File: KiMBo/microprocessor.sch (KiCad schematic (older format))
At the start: 22 parts

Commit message: Update to use OSD335x as the main chipset
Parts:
- removed C? (x3): 1μF, symbol C
- removed C? (x3): 100nF, symbol C
- removed C?: 10nF, symbol C
- removed C? (x3): 10pF, symbol C
- removed C? (x2): 4.7μF, symbol C
- removed C? (x2): 18pF, symbol C
- removed L? (x2): 3.9nH, symbol INDUCTOR
- removed R? (x2): 4.7kΩ, symbol R
- removed R?: 22Ω, symbol R
- removed U? (x2): MT7620N, symbol MT7620N
- removed X?: 20MHz, symbol CRYSTAL-4
- added C? (x4): CP1, symbol CP1
- added R? (x2): R, symbol R
- added U? (x7): OSD3358, symbol OSD3358
- added Y? (x2): CRYSTAL, symbol CRYSTAL
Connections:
- net labels added: JTAG_FMJ0, JTAG_FMJ1, JTAG_TCK, JTAG_TDI, JTAG_TDO, JTAG_TMS, JTAG_TRSTN
- net labels removed: +1V2, +1V8, +3V3, 12S_CTRL, DDR_VREF, ERROR_LED, GND, MT_PLL_VC_CAP, MT_XTAL_XI, MT_XTAL_XO, RF0_V33N, RF1_V33N, ~PORST
- wire segments 111 -> 49
- no-connect marks 6 -> 1
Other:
- note added: "Analog I/O"
- note added: "EMMC04G-S100-B08U"
- note added: "GPMC"
- note added: "JTAG"
- note added: "LCD"

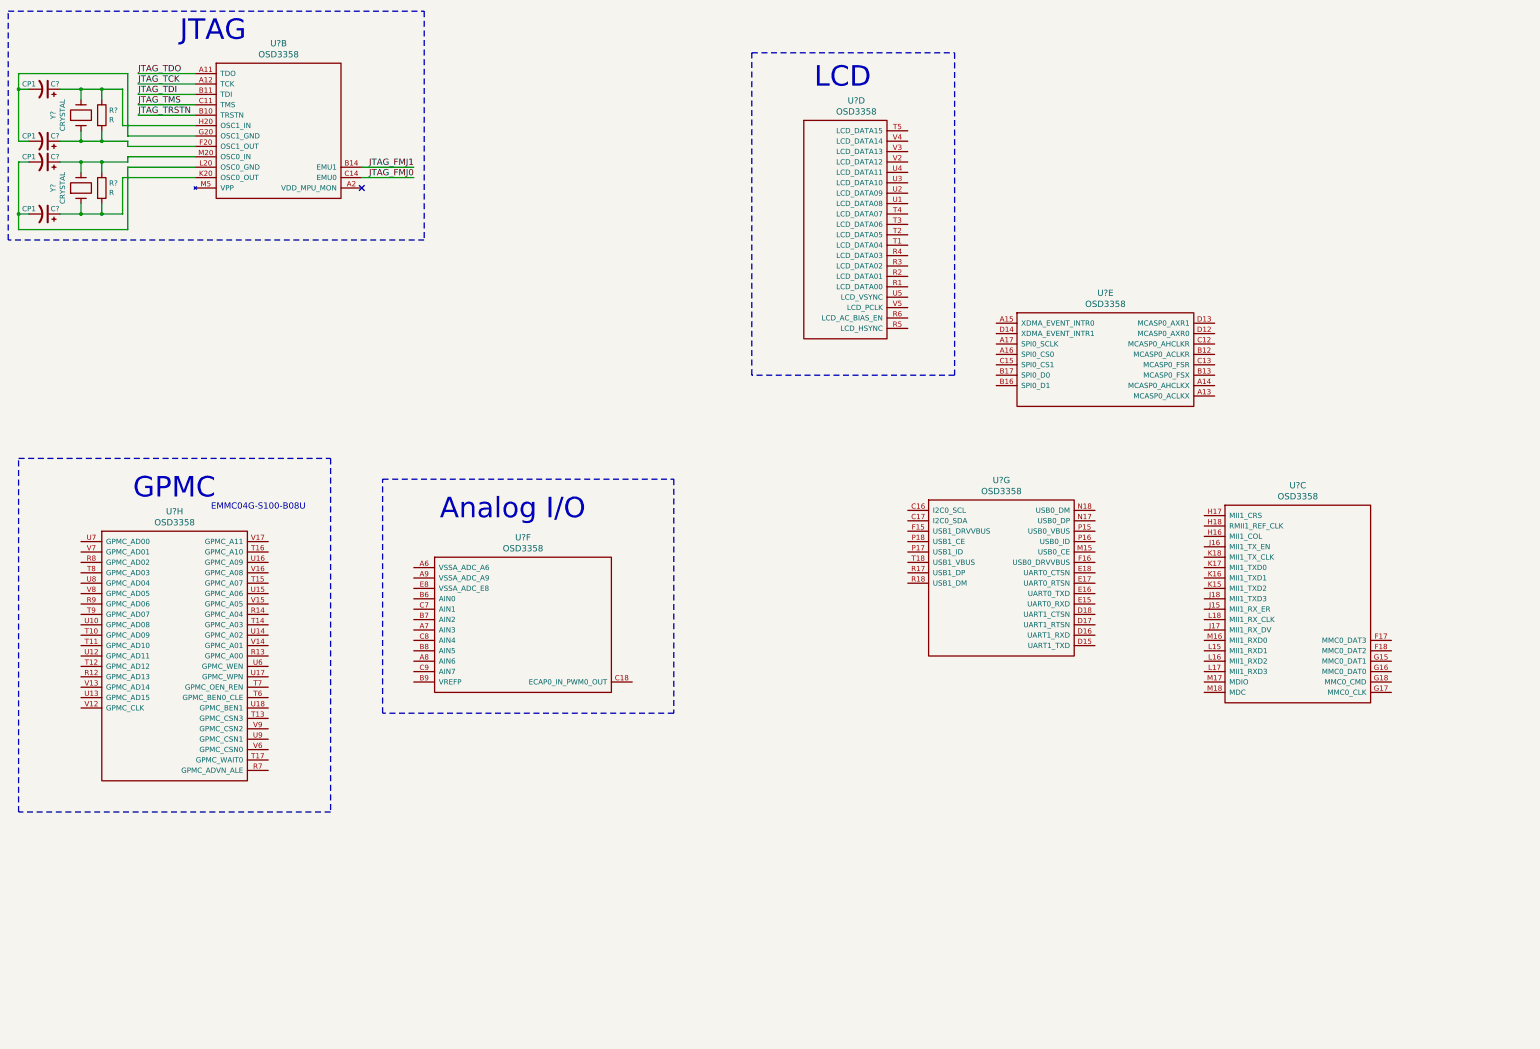
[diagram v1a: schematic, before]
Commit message: Move various symbols, add notes, add labels
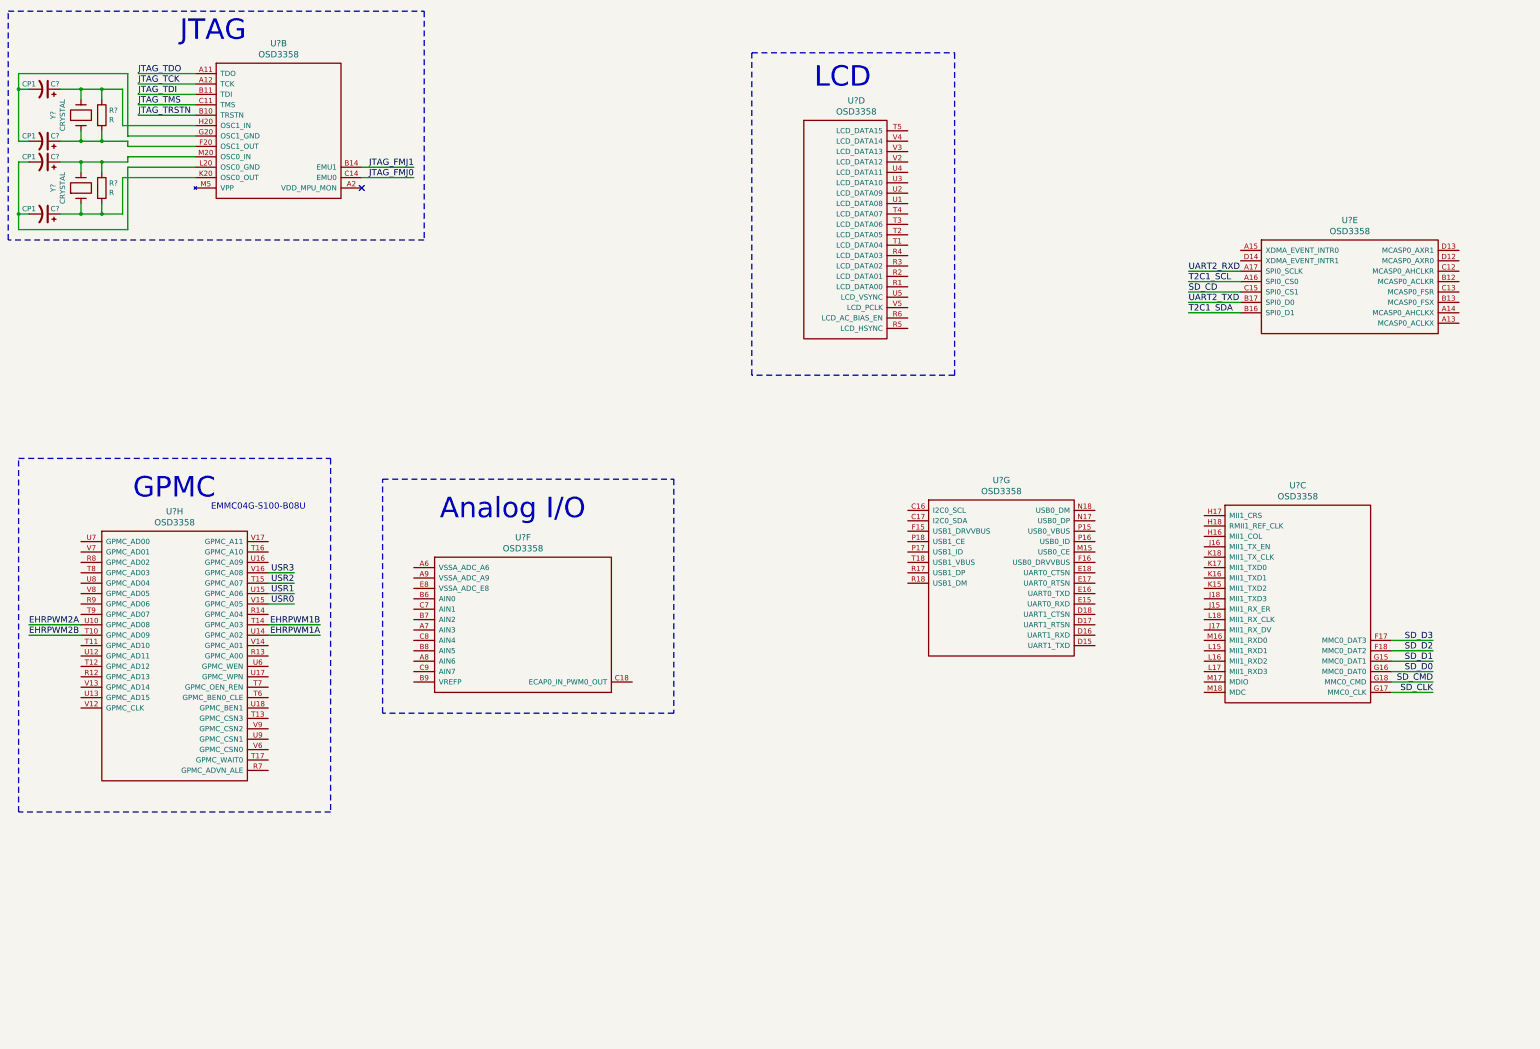
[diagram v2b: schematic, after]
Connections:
- net EHRPWM2B: now reaches U?.T10 (GPMC_AD09)
- net EHRPWM1B: now reaches U?.T14 (GPMC_A03)
- net USR2: now reaches U?.T15 (GPMC_A07)
- net EHRPWM2A: now reaches U?.U10 (GPMC_AD08)
- net EHRPWM1A: now reaches U?.U14 (GPMC_A02)
- net USR1: now reaches U?.U15 (GPMC_A06)
- net USR0: now reaches U?.V15 (GPMC_A05)
- net USR3: now reaches U?.V16 (GPMC_A08)
- net T2C1_SCL: now reaches U?.A16 (SPI0_CS0)
- net UART2_RXD: now reaches U?.A17 (SPI0_SCLK)
- net T2C1_SDA: now reaches U?.B16 (SPI0_D1)
- net UART2_TXD: now reaches U?.B17 (SPI0_D0)
- net SD_CD: now reaches U?.C15 (SPI0_CS1)
- net SD_D3: now reaches U?.F17 (MMC0_DAT3)
- net SD_D2: now reaches U?.F18 (MMC0_DAT2)
- net SD_D1: now reaches U?.G15 (MMC0_DAT1)
- net SD_D0: now reaches U?.G16 (MMC0_DAT0)
- net SD_CLK: now reaches U?.G17 (MMC0_CLK)
- net SD_CMD: now reaches U?.G18 (MMC0_CMD)
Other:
- moved on the sheet: U?E
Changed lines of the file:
@@
 L OSD3358 U?
 U 5 1 582FE5A0
-P 10250 3700
-F 0 "U?" H 11300 3990 60  0000 C CNN
-F 1 "OSD3358" H 11300 3884 60  0000 C CNN
-F 2 "" H 10250 3700 60  0001 C CNN
-F 3 "" H 10250 3700 60  0001 C CNN
-	5    10250 3700
+P 12600 3000
+F 0 "U?" H 13650 3290 60  0000 C CNN
+F 1 "OSD3358" H 13650 3184 60  0000 C CNN
+F 2 "" H 12600 3000 60  0001 C CNN
+F 3 "" H 12600 3000 60  0001 C CNN
+	5    12600 3000
 	1    0    0    -1
 $EndComp
@@
 	850  2650 950  2650
 Wire Wire Line
-	850  2150 850  2650
-Wire Wire Line
-	850  2650 850  2800
+	850  2150 850  2800
 Wire Wire Line
 	950  2150 850  2150
@@
 	850  1950 950  1950
 Wire Wire Line
-	850  1300 850  1450
-Wire Wire Line
-	850  1450 850  1950
+	850  1300 850  1950
 Wire Wire Line
 	850  1450 950  1450
@@
 $EndComp
 Wire Wire Line
-	1900 1950 1650 1950
-Wire Wire Line
-	1650 1950 1450 1950
-Wire Wire Line
-	1450 1950 1250 1950
-Wire Wire Line
-	1850 1450 1650 1450
-Wire Wire Line
-	1650 1450 1450 1450
-Wire Wire Line
-	1450 1450 1250 1450
-Wire Wire Line
-	1250 2650 1450 2650
-Wire Wire Line
-	1450 2650 1650 2650
-Wire Wire Line
-	1650 2650 1850 2650
-Wire Wire Line
-	1250 2150 1450 2150
-Wire Wire Line
-	1450 2150 1650 2150
-Wire Wire Line
-	1650 2150 1900 2150
+	1900 1950 1250 1950
+Wire Wire Line
+	1850 1450 1250 1450
+Wire Wire Line
+	1250 2650 1850 2650
+Wire Wire Line
+	1250 2150 1900 2150
 Wire Wire Line
 	1450 2250 1450 2150
@@
 	1450 1850 1450 1950
 Connection ~ 1450 1950
+Text Label 3500 6400 2    60   ~ 0
+USR0
+Text Label 3500 6300 2    60   ~ 0
+USR1
+Wire Wire Line
+	3500 6300 3250 6300
+Wire Wire Line
+	3250 6400 3500 6400
+Text Label 3500 6200 2    60   ~ 0
+USR2
+Text Label 3500 6100 2    60   ~ 0
+USR3
+Wire Wire Line
+	3250 6100 3500 6100
+Wire Wire Line
+	3250 6200 3500 6200
+Text Label 12100 3200 0    60   ~ 0
+UART2_RXD
+Text Label 12100 3500 0    60   ~ 0
+UART2_TXD
+Wire Wire Line
+	12600 3200 12100 3200
+Wire Wire Line
+	12600 3500 12100 3500
+Text Label 12100 3600 0    60   ~ 0
+T2C1_SDA
+Wire Wire Line
+	12100 3600 12600 3600
+Text Label 12100 3300 0    60   ~ 0
+T2C1_SCL
+Wire Wire Line
+	12100 3300 12600 3300
+Text Label 950  6700 0    60   ~ 0
+EHRPWM2B
+Wire Wire Line
+	1450 6700 950  6700
+Text Label 950  6600 0    60   ~ 0
+EHRPWM2A
+Text Label 3750 6600 2    60   ~ 0
+EHRPWM1B
+Text Label 3750 6700 2    60   ~ 0
+EHRPWM1A
+Wire Wire Line
+	3750 6600 3250 6600
+Wire Wire Line
+	3750 6700 3250 6700
+Wire Wire Line
+	1450 6600 950  6600
+Text Label 14450 6750 2    60   ~ 0
+SD_D3
+Text Label 14450 6850 2    60   ~ 0
+SD_D2
+Text Label 14450 6950 2    60   ~ 0
+SD_D1
+Text Label 14450 7050 2    60   ~ 0
+SD_D0
+Text Label 14450 7150 2    60   ~ 0
+SD_CMD
+Text Label 14450 7250 2    60   ~ 0
+SD_CLK
+Text Label 12100 3400 0    60   ~ 0
+SD_CD
+Wire Wire Line
+	12100 3400 12600 3400
+Wire Wire Line
+	14450 6750 14050 6750
+Wire Wire Line
+	14450 6850 14050 6850
+Wire Wire Line
+	14450 6950 14050 6950
+Wire Wire Line
+	14450 7050 14050 7050
+Wire Wire Line
+	14450 7150 14050 7150
+Wire Wire Line
+	14450 7250 14050 7250
 $EndSCHEMATC

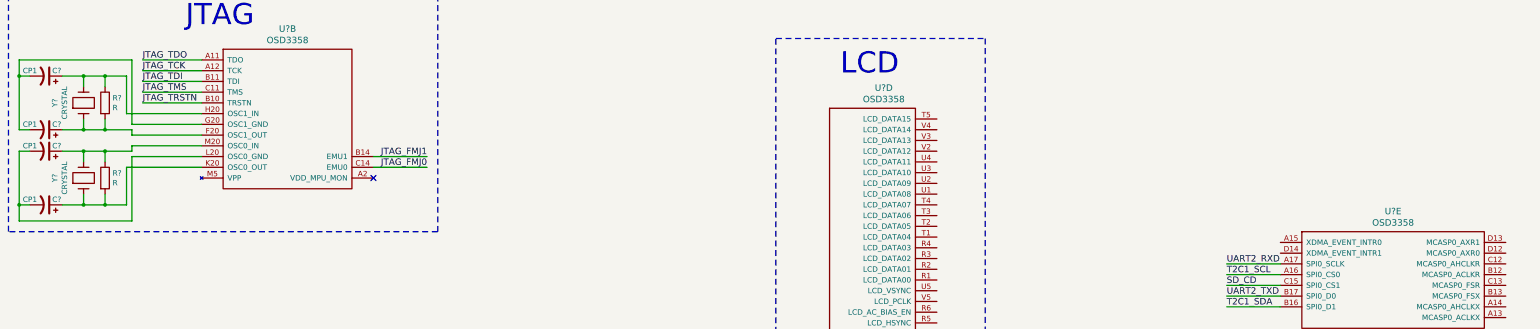
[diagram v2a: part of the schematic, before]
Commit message: Update the schematic with various nets and labels
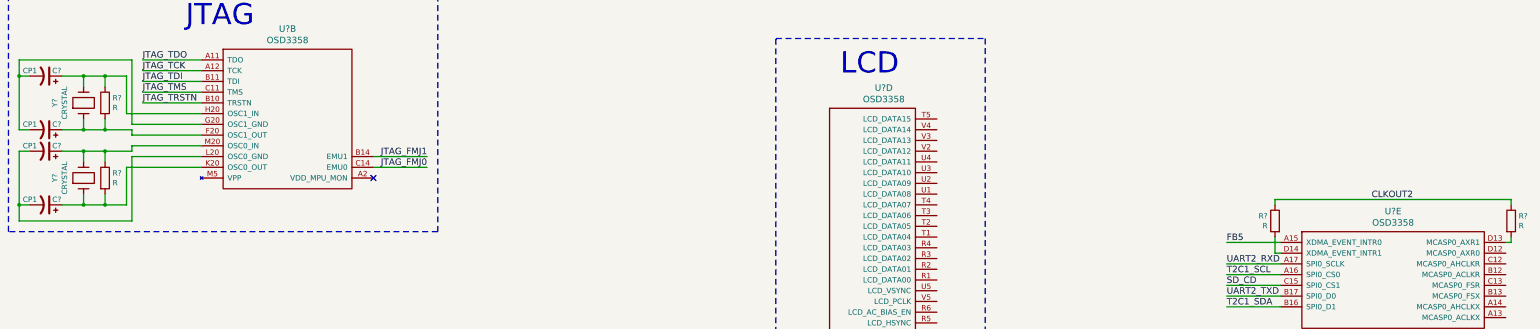
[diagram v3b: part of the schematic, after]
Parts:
- added R? (x2): R, symbol R
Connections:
- net FB5: now reaches U?.A15 (XDMA_EVENT_INTR0)
- net at U?.D13 (MCASP0_AXR1): now also R?.2
- net at U?.D14 (XDMA_EVENT_INTR1): now also R?.2
- new net CLKOUT2: R?.1, R?.1
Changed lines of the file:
@@
 	2550 2000 1900 2000
 Wire Wire Line
-	1900 2000 1900 1950
+	1900 1950 1900 2000
 Wire Wire Line
 	1900 2150 1900 2100
@@
 	2550 1800 1850 1800
 Wire Wire Line
-	1850 1800 1850 1450
+	1850 1450 1850 1800
 Wire Wire Line
 	1650 1550 1650 1450
@@
 $EndComp
 Wire Wire Line
-	1900 1950 1250 1950
-Wire Wire Line
-	1850 1450 1250 1450
+	1250 1950 1900 1950
+Wire Wire Line
+	1250 1450 1850 1450
 Wire Wire Line
 	1250 2650 1850 2650
@@
 Wire Wire Line
 	14450 7250 14050 7250
+$Comp
+L R R?
+U 1 1 5834D6F6
+P 14750 2800
+F 0 "R?" H 14820 2846 50  0000 L CNN
+F 1 "R" H 14820 2755 50  0000 L CNN
+F 2 "" V 14680 2800 50  0000 C CNN
+F 3 "" H 14750 2800 50  0000 C CNN
+	1    14750 2800
+	1    0    0    -1
+$EndComp
+Wire Wire Line
+	14700 3000 14750 3000
+Wire Wire Line
+	14750 3000 14750 2950
+$Comp
+L R R?
+U 1 1 5834D7CD
+P 12550 2800
+F 0 "R?" H 12619 2846 50  0000 L CNN
+F 1 "R" H 12619 2755 50  0000 L CNN
+F 2 "" V 12480 2800 50  0000 C CNN
+F 3 "" H 12550 2800 50  0000 C CNN
+	1    12550 2800
+	-1   0    0    -1
+$EndComp
+Wire Wire Line
+	12600 3100 12550 3100
+Wire Wire Line
+	12550 3100 12550 2950
+Wire Wire Line
+	12550 2650 12550 2600
+Wire Wire Line
+	12550 2600 14750 2600
+Wire Wire Line
+	14750 2600 14750 2650
+Text Label 13450 2600 0    60   ~ 0
+CLKOUT2
+Wire Wire Line
+	12600 3000 12100 3000
+Text Label 12100 3000 0    60   ~ 0
+FB5
 $EndSCHEMATC

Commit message: More updates to the schematics
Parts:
- added C?: C, symbol C
- added C? (x3): CP1, symbol CP1
- added OSC?: ASDMB, symbol ASDMB
- added P?: CONN_01X06, symbol CONN_01X06
- added R? (x18): R, symbol R
- added U?: 74LVC1G06, symbol 74LVC1G06
- added U?: 74LVC2G241, symbol 74LVC2G241
- added U?: 74LVC1G74, symbol 74LVC1G74
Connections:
- net FB5: now also R?.2
- net GPIO1_13: now reaches U?.R12 (GPMC_AD13)
- net GPIO1_16.SIP: now reaches U?.R13 (GPMC_A00)
- net GPIO1_16.SIP: now also R?.1
- net at U?.R14 (GPMC_A04): now also U?.2
- net TIMER4: now reaches U?.R7 (GPMC_ADVN_ALE)
- net MMC1_DAT2: now reaches U?.R8 (GPMC_AD02)
- net MMC1_DAT6: now reaches U?.R9 (GPMC_AD06)
- net GPIO0_26: now reaches U?.T11 (GPMC_AD10)
- net GPIO1_12: now reaches U?.T12 (GPMC_AD12)
- net GPIO2_0.SIP: now reaches U?.T13 (GPMC_CSN3)
- net USB1_OC#: now reaches U?.T16 (GPMC_A10)
- net UART4_RXD: now reaches U?.T17 (GPMC_WAIT0)
- net TIMER5: now reaches U?.T6 (GPMC_BEN0_CLE)
- net TIMER7: now reaches U?.T7 (GPMC_OEN_REN)
- net MMC1_DAT3: now reaches U?.T8 (GPMC_AD03)
- net MMC1_DAT7: now reaches U?.T9 (GPMC_AD07)
- net GPIO0_27: now reaches U?.U12 (GPMC_AD11)
- net GPIO1_15: now reaches U?.U13 (GPMC_AD15)
- net HDMI_INT: now reaches U?.U16 (GPMC_A09)
- net UART4_TXD: now reaches U?.U17 (GPMC_WPN)
- net GPIO1_28: now reaches U?.U18 (GPMC_BEN1)
- net TIMER6: now reaches U?.U6 (GPMC_WEN)
- net MMC1_DAT0: now reaches U?.U7 (GPMC_AD00)
- net MMC1_DAT4: now reaches U?.U8 (GPMC_AD04)
- net MMC1_CLK: now reaches U?.U9 (GPMC_CSN1)
- net GPIO2_1: now reaches U?.V12 (GPMC_CLK)
- net GPIO1_14: now reaches U?.V13 (GPMC_AD14)
- net GPIO1_17: now reaches U?.V14 (GPMC_A01)
- net HDMICLK_DIS#: now reaches U?.V17 (GPMC_A11)
- net HDMICLK_DIS#: now also OSC?.1 (INH#)
- net GPIO1_29: now reaches U?.V6 (GPMC_CSN0)
- net MMC1_DAT1: now reaches U?.V7 (GPMC_AD01)
- net MMC1_DAT5: now reaches U?.V8 (GPMC_AD05)
- net MMC1_CMD: now reaches U?.V9 (GPMC_CSN2)
- net GND: now reaches U?.A6 (VSSA_ADC_A6)
- net GND: now also U?.A9 (VSSA_ADC_A9), U?.E8 (VSSA_ADC_E8), C?.2, C?.2, C?.2, C?.2, OSC?.2 (GND), P?.1 (P1), R?.2, R?.2, R?.2, U?.1 (1~OE), U?.3, U?.4 (GND), U?.4 (GND)
- net AIN3: now reaches U?.A7 (AIN3)
- net AIN6: now reaches U?.A8 (AIN6)
- net AIN0: now reaches U?.B6 (AIN0)
- net AIN2: now reaches U?.B7 (AIN2)
- net AIN5: now reaches U?.B8 (AIN5)
- net VCC: now reaches U?.B9 (VREFP)
- net VCC: now also C?.1, C?.1, C?.1, C?.1, OSC?.4 (VCC), R?.1, R?.1, R?.1, R?.1, U?.5, U?.6 (~R~d), U?.7 (2OE), U?.7 (~S~d), U?.8 (VCC), U?.8 (VCC)
- net at U?.C18 (ECAP0_IN_PWM0_OUT): now also R?.2
- net AIN1: now reaches U?.C7 (AIN1)
- net AIN4: now reaches U?.C8 (AIN4)
- net at U?.C9 (AIN7): now also R?.1, R?.2
- net SPI1_SCLK: now reaches U?.A13 (MCASP0_ACLKX)
- net GPIO3_21: now reaches U?.A14 (MCASP0_AHCLKX)
- net GPIO3_21: now also R?.1
- net at U?.B12 (MCASP0_ACLKR): now also R?.2
- net SPI1_D0: now reaches U?.B13 (MCASP0_FSX)
- net SPI1_CS0: now reaches U?.C12 (MCASP0_AHCLKR)
- net GPIO3_19: now reaches U?.C13 (MCASP0_FSR)
- net SPI1_D1: now reaches U?.D12 (MCASP0_AXR0)
- net I2C0_SCL: now reaches U?.C16 (I2C0_SCL)
- net I2C0_SCL: now also R?.2
- net I2C0_SDA: now reaches U?.C17 (I2C0_SDA)
- net I2C0_SDA: now also R?.2
- net UART1_TXD: now reaches U?.D15 (UART1_TXD)
- net UART1_RXD: now reaches U?.D16 (UART1_RXD)
- net I2C2_SCL: now reaches U?.D17 (UART1_RTSN)
- net I2C2_SDA: now reaches U?.D18 (UART1_CTSN)
- net UART0_RXD: now reaches U?.E15 (UART0_RXD)
- net UART0_RXD: now also U?.6 (Y1)
- net UART0_TXD: now reaches U?.E16 (UART0_TXD)
- net UART0_TXD: now also U?.5 (2A)
- net UART0_RST#: now reaches U?.E17 (UART0_RTSN)
- net USB1_DRVVBUS: now reaches U?.F15 (USB1_DRVVBUS)
- net USB.CLIENT.D+: now reaches U?.N17 (USB0_DP)
- net USB.CLIENT.D-: now reaches U?.N18 (USB0_DM)
- net at U?.P15 (USB0_VBUS): now also R?.2
- net USB.CLIENT.ID: now reaches U?.P16 (USB0_ID)
- net at U?.P17 (USB1_ID): now also R?.1
- net USB.HOST.D+: now reaches U?.R17 (USB1_DP)
- net USB.HOST.D-: now reaches U?.R18 (USB1_DM)
- net USB1_VBUS: now reaches U?.T18 (USB1_VBUS)
- net WL_SDIO_D3.SIP: now reaches U?.H16 (MII1_COL)
- net NC2: now reaches U?.H17 (MII1_CRS)
- net WL_IR0.SIP: now reaches U?.H18 (RMII1_REF_CLK)
- net NC4: now reaches U?.J15 (MII1_RX_ER)
- net WL_SDIO_CMD.SIP: now reaches U?.J16 (MII1_TX_EN)
- net WL_SDIO_D0.SIP: now reaches U?.J17 (MII1_RX_DV)
- net WL_SDIO_D1.SIP: now reaches U?.J18 (MII1_TXD3)
- net WL_SDIO_D2.SIP: now reaches U?.K15 (MII1_TXD2)
- net NC1: now reaches U?.K16 (MII1_TXD1)
- net BT_EN.SIP: now reaches U?.K17 (MII1_TXD0)
- net WL_EN.SIP: now reaches U?.K18 (MII1_TX_CLK)
- net WL_SDIO_CLK.SIP: now reaches U?.L15 (MII1_RXD1)
- net BT_HCI_TX.SIP: now reaches U?.L16 (MII1_RXD2)
- net BT_HCI_RX.SIP: now reaches U?.L17 (MII1_RXD3)
- net LS_BUF_OE: now reaches U?.L18 (MII1_RX_CLK)
- net NC3: now reaches U?.M16 (MII1_RXD0)
- net BT_HCI_CTS.SIP: now reaches U?.M17 (MDIO)
- net BT_HCI_RTS.SIP: now reaches U?.M18 (MDC)
- net LCD.D0.B0--B3: now reaches U?.R1 (LCD_DATA00)
- net LCD.D1.B1--B4: now reaches U?.R2 (LCD_DATA01)
- net LCD.D2.B2--B5: now reaches U?.R3 (LCD_DATA02)
- net LCD.D3.B3--B6: now reaches U?.R4 (LCD_DATA03)
- net MCUJ_CD.HS: now reaches U?.R5 (LCD_HSYNC)
- net MCUJ_CD.HS: now also R?.2
- net MCUJ_CD.EN: now reaches U?.R6 (LCD_AC_BIAS_EN)
- net MCUJ_CD.EN: now also R?.2
- net LCD.D4.B4--B7: now reaches U?.T1 (LCD_DATA04)
- net LCD.D5.G0--G2: now reaches U?.T2 (LCD_DATA05)
- net LCD.D6.G1--G3: now reaches U?.T3 (LCD_DATA06)
- net LCD.D7.G2--G4: now reaches U?.T4 (LCD_DATA07)
- net LCD.D15.R4--R7: now reaches U?.T5 (LCD_DATA15)
- net LCD.D8.G3--G5: now reaches U?.U1 (LCD_DATA08)
- net LCD.D9.G4--G6: now reaches U?.U2 (LCD_DATA09)
- net LCD.D10.G5--G7: now reaches U?.U3 (LCD_DATA10)
- net LCD.D11.R0--R3: now reaches U?.U4 (LCD_DATA11)
- net MCUJ_CD.VS: now reaches U?.U5 (LCD_VSYNC)
- net MCUJ_CD.VS: now also R?.2
- net LCD.D12.R1--R4: now reaches U?.V2 (LCD_DATA12)
- net LCD.D13.R2--R5: now reaches U?.V3 (LCD_DATA13)
- net LCD.D14.R3--R6: now reaches U?.V4 (LCD_DATA14)
- net MCUJ_CD.CLK: now reaches U?.V5 (LCD_PCLK)
- net MCUJ_CD.CLK: now also R?.2
- new net: R?.2, U?.4
- new net: OSC?.3 (OUT), R?.2
- new net: P?.4 (P4), R?.1, U?.2 (1A)
- new net: P?.5 (P5), U?.3 (2Y)
- new net: R?.1, U?.5 (Q)
- new net 12MHz: R?.2
- new net 12M_LOOP: U?.2 (D), U?.3 (~Q)
- new net EMMC_RSIN: R?.1
- new net GPIO0_7: R?.1, R?.1
- new net GPIO1_16: R?.2
- new net LCD.CLOCK: R?.1
- new net LCD.ENABLE: R?.1
- new net LCD.HSYNC: R?.1
- new net LCD.VSYNC: R?.1
- new net XDMA_EVENT_INTRO: R?.1, U?.1 (Cp)
- no-connect marks 1 -> 8
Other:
- moved on the sheet: R?, U?C, U?D, U?E, U?F, U?G, U?H
